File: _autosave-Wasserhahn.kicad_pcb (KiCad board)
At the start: 2 copper layers, 76.2 x 78.1 mm, 18 parts, among them J1 Mains, J2 Ball_Valve_Contacts, J3 ToRelais, J4 PRGM_ADAPTER, J5 Boot/PRGM, U1 ESP-WROOM-02

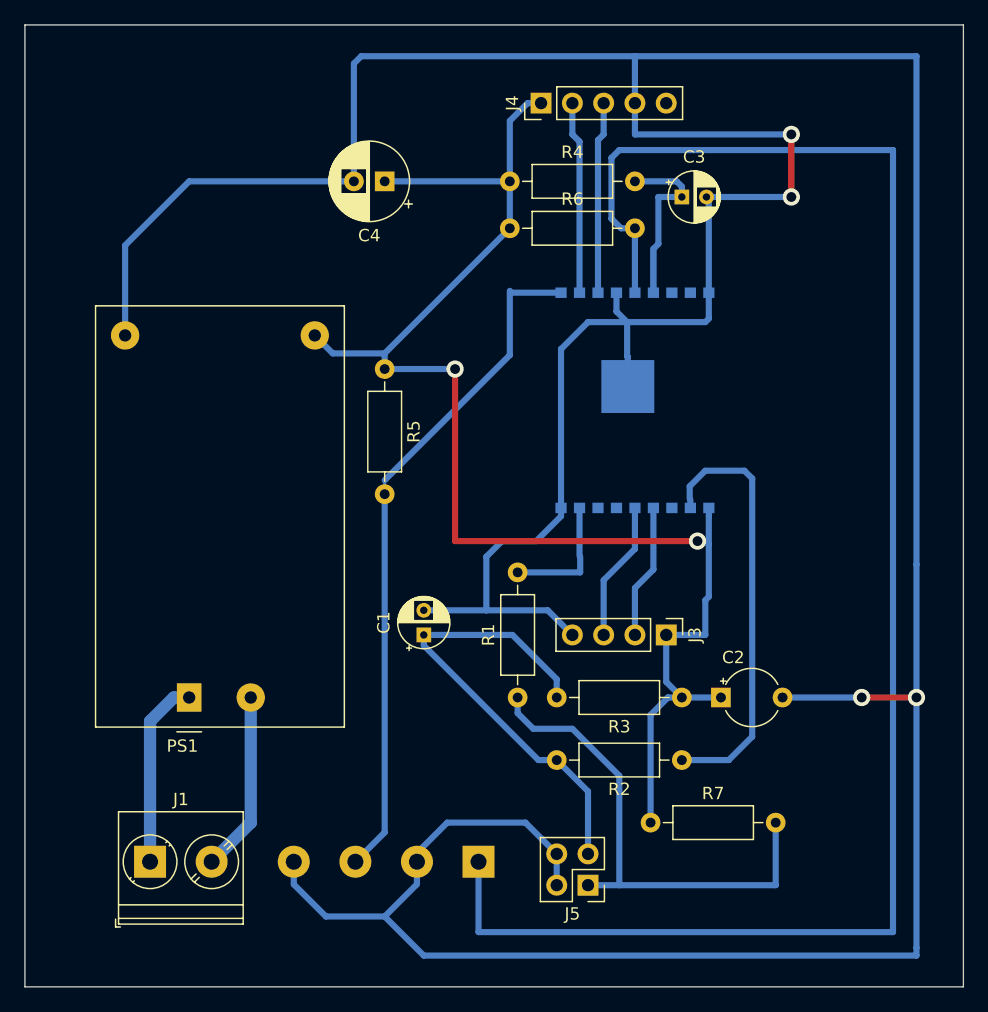
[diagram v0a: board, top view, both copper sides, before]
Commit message: optimized path in flatcam and widened the track width in kiCad
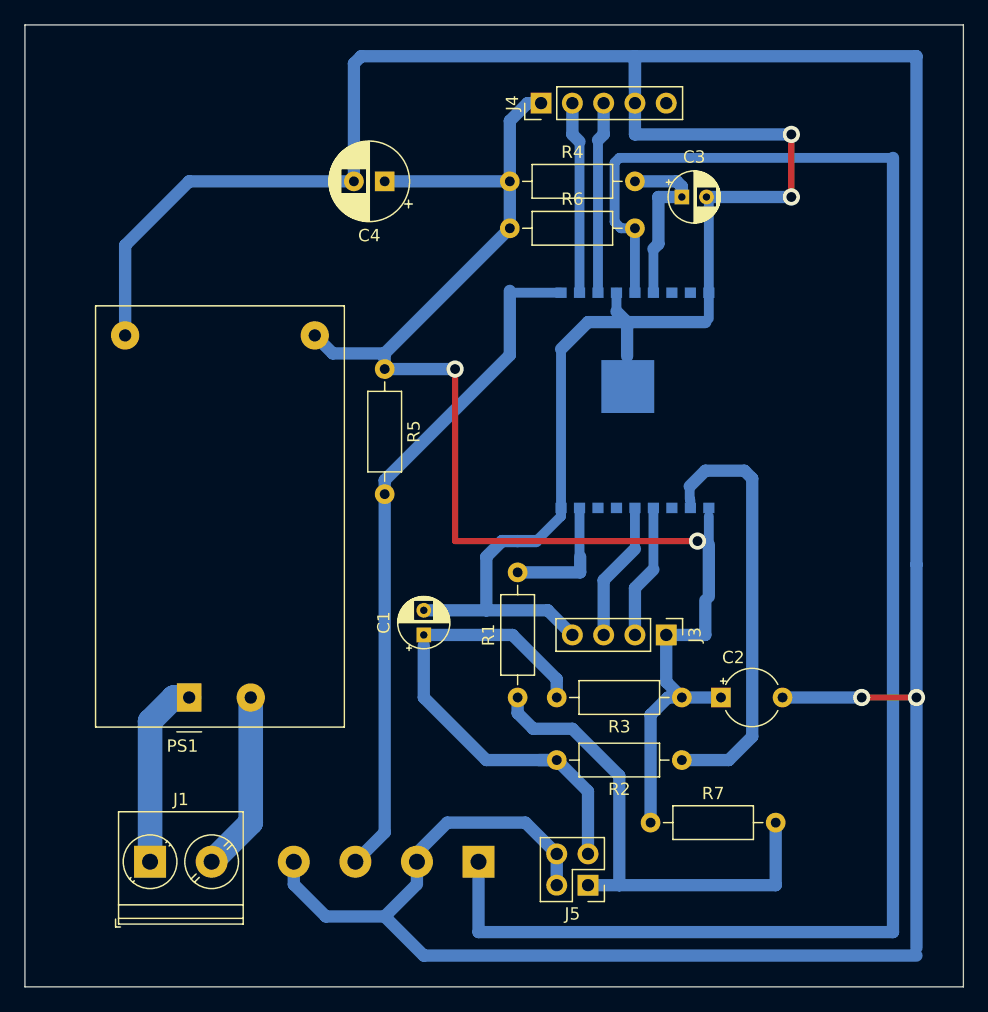
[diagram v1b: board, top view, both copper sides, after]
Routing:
- net Net-(C1-Pad1): track 37.9 -> 41.9 mm
- net /Input_Open: track 138.4 -> 136.9 mm
